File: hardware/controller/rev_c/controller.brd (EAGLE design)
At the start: 68.1 x 80 mm, 106 parts, among them J1 DM3AT-SF-PEJM5, J10 SOLDERJUMPERTRACE, J11 SOLDERJUMPERTRACE, J12 SOLDERJUMPERTRACE, J14 TC2030-JLINK-L, J15 TC2030-JLINK-L, J16 U.FL-R-SMT, J2 MICRO_USB_B_HIROSE_ZX62R-B-5P, J3 MICRO_USB_B_HIROSE_ZX62R-B-5P, J4 MODULE_CONTROLLER, J9 SOLDERJUMPERTRACE, Q1 DMN32D2LDF, SW1 B3U-1000P, SW2 B3U-1000P, SW3 SIP3240X, SW4 SIP3240X, SW5 SIP3240X, SW6 B3U-1000P, SW7 B3U-1000P, U1 FM25CLXXB-DG, U2 FTDI234XD, U3 RXM-GPS-RM-T, U33 NCP301LSN30, U4 SAM4LC8BA, U5 SAM4LC8BA, U6 SN74LVC1G125DBVR, U7 TS3USB30E, U8 TXS0108EVQFN20, U9 NCP301LSN30, X1 16MHz, X2 16MHz

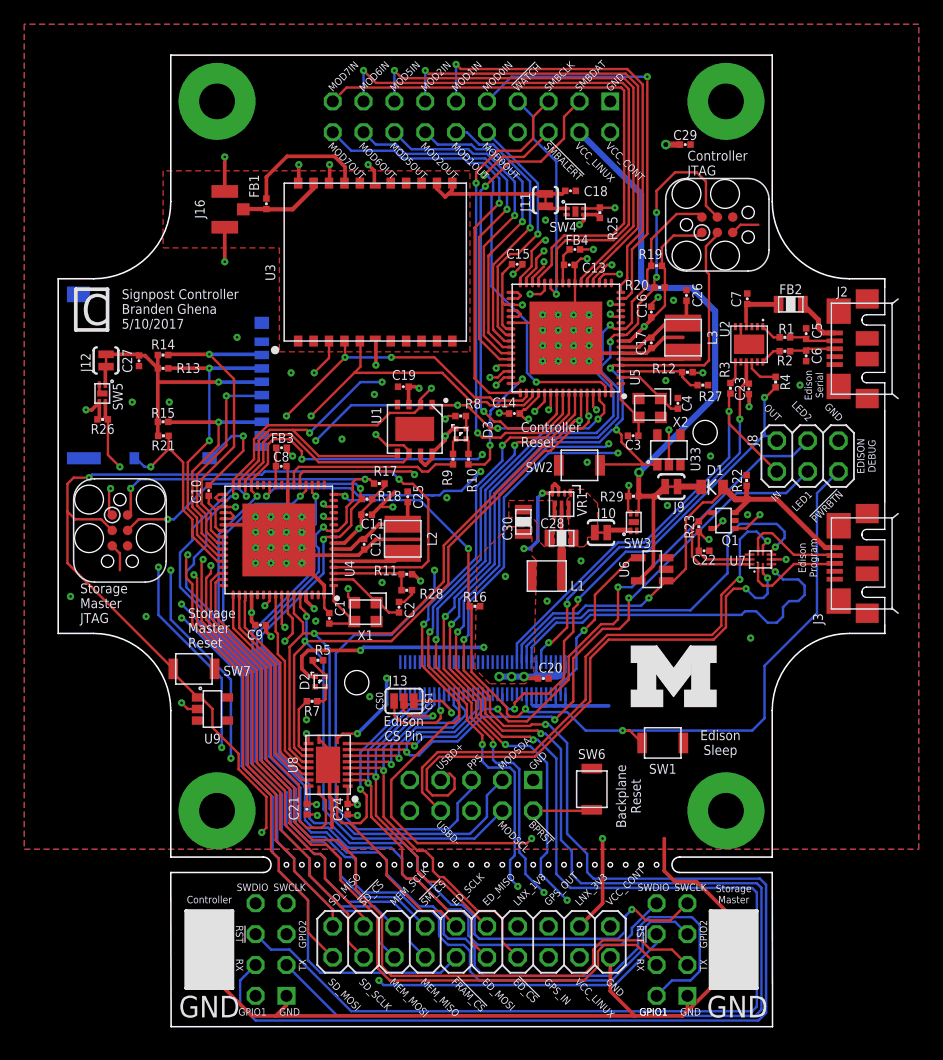
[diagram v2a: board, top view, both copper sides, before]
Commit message: Renumbered parts
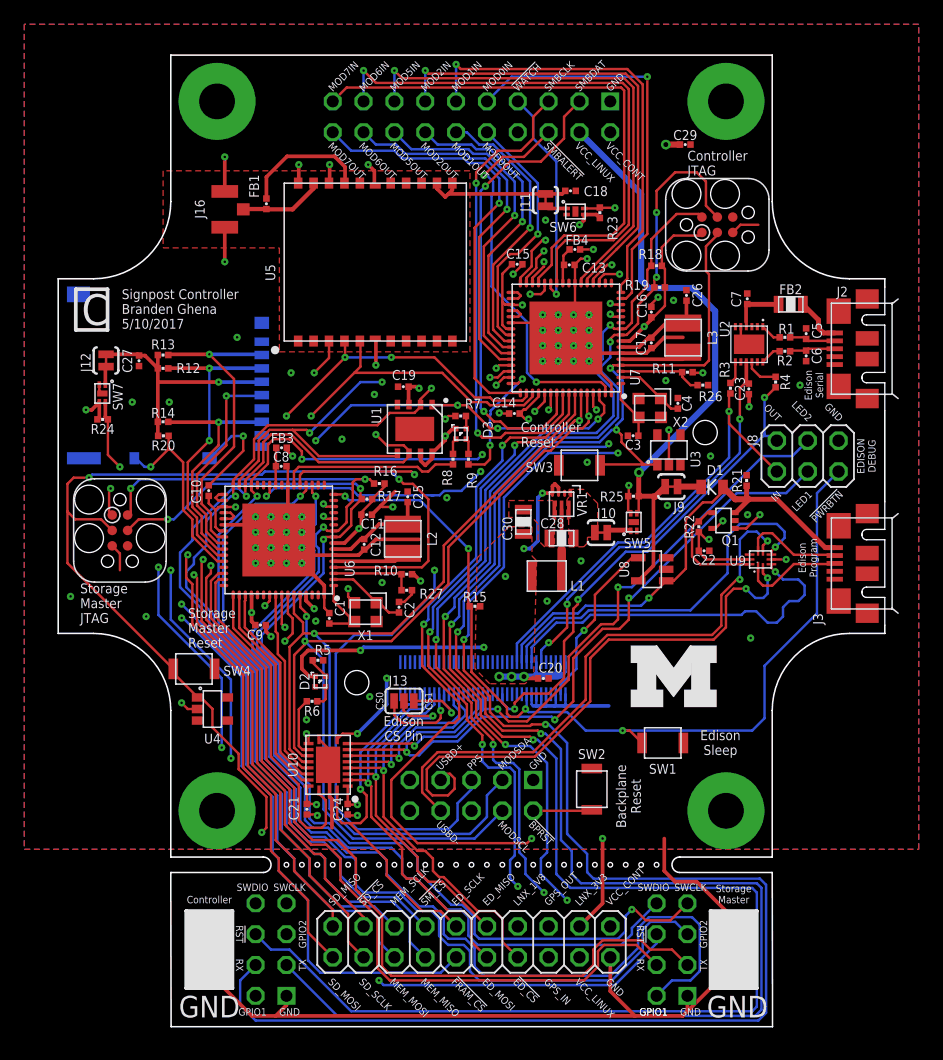
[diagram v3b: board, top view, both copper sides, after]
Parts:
- removed R28: DNP, passives:0402_RES
- removed R29: 1MΩ, passives:0402_RES
- removed U33: NCP301LSN30, signpost:SOT23-5
- added R24: 1MΩ, passives:0402_RES
- added R6: 1kΩ, passives:0402_RES
- added U10: TXS0108EVQFN20, chips:R-PVQFN-N20
- R10: value 1kΩ -> 10kΩ
- R16: value 10kΩ -> 100kΩ
- R23: value 100kΩ -> 1MΩ
- R26: value 1MΩ -> DNP
- SW3, SW4: value SIP3240X -> B3U-1000P; device signpost:TDFN4 -> switches:B3U-1000P
- SW6, SW7: value B3U-1000P -> SIP3240X; device switches:B3U-1000P -> signpost:TDFN4
- U3: value RXM-GPS-RM-T -> NCP301LSN30; device chips:RXM-GPS-RM-T -> signpost:SOT23-5
- U4: value SAM4LC8BA -> NCP301LSN30; device chips:QFN-64-9MM -> signpost:SOT23-5
- U5: value SAM4LC8BA -> RXM-GPS-RM-T; device chips:QFN-64-9MM -> chips:RXM-GPS-RM-T
- U6: value SN74LVC1G125DBVR -> SAM4LC8BA; device chips:SOT-23-5 -> chips:QFN-64-9MM
- U7: value TS3USB30E -> SAM4LC8BA; device signpost:UQFN-10 -> chips:QFN-64-9MM
- U8: value TXS0108EVQFN20 -> SN74LVC1G125DBVR; device chips:R-PVQFN-N20 -> chips:SOT-23-5
- U9: value NCP301LSN30 -> TS3USB30E; device signpost:SOT23-5 -> signpost:UQFN-10
- moved R26 49.5 mm to (19.1, 5.84)
- moved SW4 49.1 mm to (-22.9, -17.5), turned to 0 degrees
- moved R21 48.2 mm to (22.7, -2.01), turned to 90 degrees
- moved SW6 47.6 mm to (8.56, 20.1), turned to 270 degrees
- moved U9 46.8 mm to (23.8, -8.51), turned to 0 degrees
- moved SW5 45.0 mm to (13.4, -5.44), turned to 0 degrees
- moved R12 43.2 mm to (-25.4, 7.22), turned to 180 degrees
- moved R20 42.7 mm to (-25.4, 1.67), turned to 180 degrees
- moved U8 31.2 mm to (14.9, -9.32)
- moved U6 30.9 mm to (-15.9, -6.91), turned to 180 degrees
- moved R18 30.6 mm to (15.2, 15.7)
- moved R15 29.8 mm to (0.28, -12.4), turned to 0 degrees
- moved R27 29.7 mm to (-5.33, -11.0)
- moved U3 28.7 mm to (16.3, 0.51), turned to 180 degrees
- moved R11 28.5 mm to (17.8, 6.91)
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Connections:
- net !BACKPLANE_RESET: now also SW2.1, U6.58; no longer SW6.1, U4.58
- net !CONTROLLER_LED: now also R9.2, U7.48; no longer R10.2, U5.48
- net !CONTROLLER_RESET: now also SW3.1, U3.1, U7.4; no longer SW2.1, U33.1, U5.4
- net !EDISON_PWRBTN: now also R15.1, U6.16; no longer R16.1, U4.16
- net !EDISON_SPI_CS: now also U10.16, U6.56; no longer U4.56, U8.16
- net !EDISON_SPI_CS_1V8: now also U10.5; no longer U8.5
- net !ENABLE_LINUX: now also U6.21; no longer U4.21
- net !FRAM_CS: now also U7.62; no longer U5.62
- net !SD_CS: now also R13.1, U6.40; no longer R14.1, U4.40
- net !SD_DETECT: now also R20.1, U6.44; no longer R21.1, U4.44
- net !SMBALERT: now also U7.63; no longer U5.63
- net !STORAGE_CS: now also U6.29, U7.54; no longer U4.29, U5.54
- net !STORAGE_LED: now also R8.2, U6.22; no longer R9.2, U4.22
- net !STORAGE_RESET: now also SW4.1, U4.1, U6.4; no longer SW7.1, U4.4, U9.1
- net !WATCHDOG: now also U7.27; no longer U5.27
- net CONTROLLER_BUCK/LDO_N: now also R11.1, R26.2, U7.3; no longer R12.1, R27.2, U5.3
- net CONTROLLER_DEBUG_GPIO1: now also U7.57; no longer U5.57
- net CONTROLLER_DEBUG_GPIO2: now also U7.58; no longer U5.58
- net CONTROLLER_DEBUG_RX: now also U7.19; no longer U5.19
- net CONTROLLER_DEBUG_TX: now also U7.20; no longer U5.20
- net CONTROLLER_SWDCLK: now also R19.1, U7.9; no longer R20.1, U5.9
- net CONTROLLER_SWDIO: now also R18.1, U7.10; no longer R19.1, U5.10
- net CONTROLLER_XIN: now also U7.1; no longer U5.1
- net CONTROLLER_XOUT: now also U7.2; no longer U5.2
- net EDISON_INTERRUPT: now also U10.12, U6.57; no longer U4.57, U8.12
- net EDISON_INTERRUPT_1V8: now also U10.9; no longer U8.9
- net EDISON_LED1: now also U10.8; no longer U8.8
- net EDISON_SPI_MISO: now also U10.17, U6.51; no longer U4.51, U8.17
- net EDISON_SPI_MISO_1V8: now also U10.4; no longer U8.4
- net EDISON_SPI_MOSI: now also U10.18, U6.50; no longer U4.50, U8.18
- net EDISON_SPI_MOSI_1V8: now also U10.3; no longer U8.3
- net EDISON_SPI_SCLK: now also U10.20, U6.49; no longer U4.49, U8.20
- net EDISON_SPI_SCLK_1V8: now also U10.1; no longer U8.1
- net GND: now also R21.2, R26.1, R7.2, SW6.PAD, SW7.PAD, U10.11, U10.THERMAL, U3.3, U4.3, U5.18, U5.20, U5.21, U5.22, U6.23, U6.38, U6.6, U6.64, U6.GND, U7.23, U7.38, U7.6, U7.64, U7.GND, U8.2, U8.3, U9.4, U9.8; no longer R22.2, R28.1, R8.2, SW3.PAD, SW4.PAD, U3.18, U3.20, U3.21, U3.22, U33.3, U4.23, U4.38, U4.6, U4.64, U4.GND, U5.23, U5.38, U5.6, U5.64, U5.GND, U6.2, U6.3, U7.4, U7.8, U8.11, U8.THERMAL, U9.3
- net GPS_ENABLE_POWER: now also R23.1, SW6.4, U7.28; no longer R25.1, SW4.4, U5.28
- net GPS_IN_RX: now also U5.5, U7.51; no longer U3.5, U5.51
- net GPS_OUT_TX: now also U5.4, U7.50; no longer U3.4, U5.50
- net LINUX_ENABLE_POWER: now also R25.1, SW5.4; no longer R29.1, SW3.4
- net MEMORY_MISO: now also U6.32, U7.31; no longer U4.32, U5.31
- net MEMORY_MOSI: now also U6.31, U7.32; no longer U4.31, U5.32
- net MEMORY_SCLK: now also U6.30, U7.30; no longer U4.30, U5.30
- net MOD0_IN: now also U7.15; no longer U5.15
- net MOD0_OUT: now also U7.40; no longer U5.40
- net MOD1_IN: now also U7.16; no longer U5.16
- net MOD1_OUT: now also U7.41; no longer U5.41
- net MOD2_IN: now also U7.21; no longer U5.21
- net MOD2_OUT: now also U7.42; no longer U5.42
- net MOD5_IN: now also U7.22; no longer U5.22
- net MOD5_OUT: now also U7.43; no longer U5.43
- net MOD6_IN: now also U7.26; no longer U5.26
- net MOD6_OUT: now also U7.44; no longer U5.44
- net MOD7_IN: now also U7.29; no longer U5.29
- net MOD7_OUT: now also U7.49; no longer U5.49
- net MODSTORAGE_IN: now also U6.14, U7.46; no longer U4.14, U5.46
- net MODSTORAGE_OUT: now also U6.12, U7.47; no longer U4.12, U5.47
- net MODULES_SCL: now also U10.14, U6.60, U7.12, U7.60; no longer U4.60, U5.12, U5.60, U8.14
- net MODULES_SCL_1V8: now also U10.7; no longer U8.7
- net MODULES_SDA: now also U10.15, U6.59, U7.14, U7.59; no longer U4.59, U5.14, U5.59, U8.15
- net MODULES_SDA_1V8: now also U10.6; no longer U8.6
- net N$1: now also U5.17; no longer U3.17
- net N$16: now also SW5.1; no longer SW3.1
- net N$17: now also U8.4; no longer U6.4
- net N$18: now also SW7.1; no longer SW5.1
- net N$19: now also SW6.1; no longer SW4.1
- net N$29: now also U6.25; no longer U4.25
- net N$3: now also U5.19; no longer U3.19
- net N$30: now also R22.2, U9.10; no longer R23.2, U7.10
- net N$32: now also U7.25; no longer U5.25
- net N$38: now also R6.1; no longer R7.1
- net N$44: now also U7.7; no longer U5.7
- net N$45: now also U6.7; no longer U4.7
- net N$46: now also U6.5; no longer U4.5
- net N$48: now also U6.33, U6.34; no longer U4.33, U4.34
- net N$5: now also U9.7; no longer U7.7
- net N$50: now also R6.2, U10.13; no longer R7.2, U8.13
- net N$51: now also U6.36, U6.37; no longer U4.36, U4.37
- net N$53: now also U7.36, U7.37; no longer U5.36, U5.37
- net N$54: now also U7.33, U7.34; no longer U5.33, U5.34
- net N$56: now also U5.11, U5.12; no longer U3.11, U3.12
- net N$58: now also R12.2, R20.2; no longer R15.2, R21.2
- net N$59: now also U7.5; no longer U5.5
- net N$6: now also U9.1; no longer U7.1
- net N$7: now also R7.1; no longer R8.1
- net N$8: now also R8.1; no longer R9.1
- net N$9: now also R9.1; no longer R10.1
- net PPS: now also U5.3, U7.45; no longer U3.3, U5.45
- net SD_ENABLE_POWER: now also R24.1, SW7.4, U6.55; no longer R26.1, SW5.4, U4.55
- net SD_MISO: now also R14.1, U6.42; no longer R15.1, U4.42
- net SD_MOSI: now also R12.1, U6.43; no longer R13.1, U4.43
- net SD_SCLK: now also U6.41; no longer U4.41
- net SMBCLK: now also U7.56; no longer U5.56
- net SMBDATA: now also U7.55; no longer U5.55
- net STORAGE_BUCK/LDO_N: now also R10.1, R27.2, U6.3; no longer R11.1, R28.2, U4.3
- net STORAGE_DEBUG_GPIO1: now also U6.19; no longer U4.19
- net STORAGE_DEBUG_GPIO2: now also U6.20; no longer U4.20
- net STORAGE_DEBUG_RX: now also U6.46; no longer U4.46
- net STORAGE_DEBUG_TX: now also U6.47; no longer U4.47
- net STORAGE_INTERRUPT: now also U6.26, U7.53; no longer U4.26, U5.53
- net STORAGE_SWDCLK: now also R17.1, U6.9; no longer R18.1, U4.9
- net STORAGE_SWDIO: now also R16.1, U6.10; no longer R17.1, U4.10
- net STORAGE_XIN: now also U6.1; no longer U4.1
- net STORAGE_XOUT: now also U6.2; no longer U4.2
- net USB_D+: now also U9.3; no longer U7.3
- net USB_D-: now also U9.5; no longer U7.5
- net USB_MOD_D+: now also U9.2; no longer U7.2
- net USB_MOD_D-: now also U9.6; no longer U7.6
- net USB_VBUS: now also R21.1, U8.1; no longer R22.1, U6.1
- net VCC_CONTROLLER: now also R10.2, R16.2, R23.2, R24.2, SW6.3, SW7.3, U3.2, U4.2, U6.35, U6.39, U6.52, U6.61, U6.8, U7.35, U7.39, U7.52, U7.61, U7.8; no longer R12.2, R20.2, R25.2, R26.2, SW4.3, SW5.3, U33.2, U4.35, U4.39, U4.52, U4.61, U4.8, U5.35, U5.39, U5.52, U5.61, U5.8, U9.2
- net VCC_LINUX: now also R25.2, SW5.3, U8.5; no longer R29.2, SW3.3, U6.5
- net VCC_LINUX_1V8: now also U10.10, U10.2; no longer U8.10, U8.2
- net VCC_LINUX_3V3: now also R15.2, R22.1, U10.19, U9.9; no longer R16.2, R23.1, U7.9, U8.19

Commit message: Added updates from Pat & Josh
Pulldown on 1v8 output enable
PPS connection to storage master

Did NOT add module in/out pins for the edison
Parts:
- added R28: 100kΩ, passives:0402_RES
- moved C23 1.02 mm to (23.9, 5.54)
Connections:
- net GND: now also R28.2
- net PPS: now also U6.45
- net VCC_LINUX_1V8: now also R28.1
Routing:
- net PPS: track 76.8 -> 98.8 mm, vias 3 -> 4
- net VCC_LINUX_1V8: track 84.0 -> 85.1 mm
- net GND: track 201.9 -> 200.9 mm, vias 79 -> 78
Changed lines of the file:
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@@
 <attribute name="NAME" x="19.1516" y="-8.9408" size="0.8128" layer="25" font="vector" ratio="12" align="bottom-center"/>
 </element>
-<element name="C23" library="passives" package="0402_CAP" value="100nF" x="22.836" y="5.5372" smashed="yes" rot="R270">
-<attribute name="DIGIKEY" value="490-10777-1-ND" x="22.836" y="4.2672" size="1.778" layer="27" rot="R270" display="off"/>
-<attribute name="NAME" x="21.693" y="5.5372" size="0.8128" layer="25" font="vector" ratio="12" rot="R270" align="bottom-center"/>
+<element name="C23" library="passives" package="0402_CAP" value="100nF" x="23.852" y="5.5372" smashed="yes" rot="R270">
+<attribute name="DIGIKEY" value="490-10777-1-ND" x="23.852" y="4.2672" size="1.778" layer="27" rot="R270" display="off"/>
+<attribute name="NAME" x="22.963" y="3.7592" size="0.8128" layer="25" font="vector" ratio="12" rot="R270" align="bottom-center"/>
 </element>
 <element name="C7" library="passives" package="0402_CAP" value="10nF" x="22.709" y="12.954" smashed="yes" rot="R90">
@@
 <attribute name="NAME" x="-21.336" y="-22.86" size="0.8128" layer="25" font="vector" ratio="12" rot="R180" align="bottom-center"/>
 <attribute name="VALUE" x="-21.336" y="-18.796" size="1.016" layer="27" font="vector" ratio="12" align="bottom-center"/>
+</element>
+<element name="R28" library="passives" package="0402_RES" value="100kΩ" x="22.86" y="5.461" smashed="yes" rot="R270">
+<attribute name="DIGIKEY" value="1276-3432-1-ND" x="22.86" y="4.953" size="1.778" layer="27" rot="R270" display="off"/>
+<attribute name="NAME" x="21.717" y="4.699" size="0.8128" layer="25" font="vector" ratio="12" rot="R270" align="bottom-center"/>
+<attribute name="VALUE" x="21.463" y="5.461" size="1.016" layer="27" font="vector" ratio="12" rot="R270" align="bottom-center"/>
 </element>
 </elements>
@@
 <wire x1="22.86" y1="9.2075" x2="22.18" y2="9.8875" width="0.2032" layer="1"/>
 <wire x1="22.18" y1="9.8875" x2="22.18" y2="10.6575" width="0.2032" layer="1"/>
-<wire x1="22.836" y1="5.10413125" x2="22.86" y2="5.08013125" width="0.3048" layer="1"/>
-<wire x1="22.86" y1="5.08013125" x2="22.86" y2="4.064" width="0.3048" layer="1"/>
-<via x="22.86" y="4.064" extent="1-16" drill="0.2032"/>
 <wire x1="-20.32" y1="21.795" x2="-20.32" y2="24.638" width="0.3048" layer="1"/>
 <via x="-20.32" y="24.638" extent="1-16" drill="0.2032"/>
@@
 <wire x1="3.09753125" y1="3.5052" x2="2.3368" y2="3.5052" width="0.2032" layer="1"/>
 <wire x1="2.3368" y1="3.5052" x2="2.286" y2="3.556" width="0.2032" layer="1"/>
+<contactref element="R28" pad="2"/>
 </signal>
 <signal name="PPS">
@@
 <wire x1="-11.7348" y1="8.0772" x2="-12.954" y2="6.858" width="0.2032" layer="1"/>
 <via x="-12.954" y="6.858" extent="1-16" drill="0.2032"/>
-<wire x1="-12.954" y1="6.858" x2="0.254" y2="6.858" width="0.2032" layer="2"/>
+<wire x1="0.254" y1="6.858" x2="-12.954" y2="6.858" width="0.2032" layer="2"/>
 <via x="2.032" y="7.239" extent="1-16" drill="0.2032"/>
 <wire x1="-3.048" y1="-9.398" x2="-3.048" y2="-6.604" width="0.2032" layer="2"/>
@@
 <wire x1="2.032" y1="7.239" x2="0.635" y2="7.239" width="0.2032" layer="2"/>
 <wire x1="0.635" y1="7.239" x2="0.254" y2="6.858" width="0.2032" layer="2"/>
+<contactref element="U6" pad="45"/>
+<wire x1="-12.954" y1="6.858" x2="-12.954" y2="3.83826875" width="0.2032" layer="2"/>
+<wire x1="-12.2682" y1="-1.7018" x2="-12.192" y2="-1.778" width="0.2032" layer="2"/>
+<wire x1="-12.954" y1="3.83826875" x2="-12.2682" y2="3.15246875" width="0.2032" layer="2"/>
+<wire x1="-12.2682" y1="3.15246875" x2="-12.2682" y2="-1.7018" width="0.2032" layer="2"/>
+<wire x1="-12.192" y1="-1.778" x2="-13.1572" y2="-2.7432" width="0.2032" layer="2"/>
+<wire x1="-13.1572" y1="-2.7432" x2="-14.32846875" y2="-2.7432" width="0.2032" layer="2"/>
+<wire x1="-15.44606875" y1="-3.8608" x2="-17.78" y2="-3.8608" width="0.2032" layer="2"/>
+<wire x1="-17.78" y1="-3.8608" x2="-19.431" y2="-5.5118" width="0.2032" layer="2"/>
+<wire x1="-14.32846875" y1="-2.7432" x2="-15.44606875" y2="-3.8608" width="0.2032" layer="2"/>
+<via x="-19.431" y="-8.636" extent="1-16" drill="0.2032"/>
+<wire x1="-19.431" y1="-5.5118" x2="-19.431" y2="-8.636" width="0.2032" layer="2"/>
+<wire x1="-20.4" y1="-9.1588" x2="-19.9538" y2="-9.1588" width="0.2032" layer="1"/>
+<wire x1="-19.9538" y1="-9.1588" x2="-19.431" y2="-8.636" width="0.2032" layer="1"/>
 </signal>
 <signal name="N$1">
@@
 <via x="3.556" y="-20.828" extent="1-16" drill="0.2032"/>
 <via x="8.763" y="-11.811" extent="1-16" drill="0.2032"/>
-<via x="24.13" y="4.826" extent="1-16" drill="0.2032"/>
 <wire x1="8.763" y1="-11.811" x2="12.7" y2="-7.874" width="0.2032" layer="16"/>
 <wire x1="12.7" y1="-7.874" x2="14.478" y2="-7.874" width="0.2032" layer="16"/>
 <contactref element="J8" pad="5"/>
 <wire x1="14.478" y1="-7.874" x2="24.003" y2="1.651" width="0.2032" layer="16"/>
-<wire x1="24.003" y1="1.651" x2="24.13" y2="1.778" width="0.2032" layer="16"/>
-<wire x1="24.13" y1="1.778" x2="24.13" y2="4.826" width="0.2032" layer="16"/>
 <wire x1="25.146" y1="1.27" x2="24.765" y2="1.651" width="0.2032" layer="16"/>
 <wire x1="24.765" y1="1.651" x2="24.003" y2="1.651" width="0.2032" layer="16"/>
@@
 <wire x1="8.382" y1="-12.573" x2="8.763" y2="-12.192" width="0.2032" layer="1"/>
 <wire x1="8.763" y1="-12.192" x2="8.763" y2="-11.811" width="0.2032" layer="1"/>
-<wire x1="25.0444" y1="5.66293125" x2="24.20746875" y2="4.826" width="0.2032" layer="1"/>
-<wire x1="24.20746875" y1="4.826" x2="24.13" y2="4.826" width="0.2032" layer="1"/>
+<wire x1="25.4" y1="3.048" x2="25.4" y2="4.318" width="0.2032" layer="16"/>
+<via x="25.4" y="4.318" extent="1-16" drill="0.2032"/>
+<wire x1="25.4" y1="4.318" x2="25.0444" y2="4.6736" width="0.2032" layer="1"/>
+<wire x1="25.0444" y1="4.6736" x2="25.0444" y2="5.66293125" width="0.2032" layer="1"/>
+<wire x1="24.003" y1="1.651" x2="25.4" y2="3.048" width="0.2032" layer="16"/>
 </signal>
 <signal name="N$28">
@@
 <contactref element="C24" pad="2"/>
 <contactref element="J7" pad="14"/>
-<wire x1="22.63" y1="7.7575" x2="22.63" y2="6.17626875" width="0.3048" layer="1"/>
-<wire x1="22.63" y1="6.17626875" x2="22.836" y2="5.97026875" width="0.3048" layer="1"/>
 <wire x1="-10.1985" y1="-27.1754" x2="-10.1985" y2="-28.64993125" width="0.2032" layer="1"/>
 <wire x1="-10.1985" y1="-28.64993125" x2="-10.14643125" y2="-28.702" width="0.2032" layer="1"/>
@@
 <via x="22.098" y="3.048" extent="1-16" drill="0.2032"/>
 <wire x1="22.098" y1="3.048" x2="22.098" y2="5.588" width="0.2032" layer="1"/>
-<wire x1="22.098" y1="5.588" x2="22.48026875" y2="5.97026875" width="0.2032" layer="1"/>
-<wire x1="22.48026875" y1="5.97026875" x2="22.836" y2="5.97026875" width="0.2032" layer="1"/>
 <wire x1="6.35" y1="-17.931609375" x2="6.35" y2="-15.367" width="0.3048" layer="15"/>
 <wire x1="6.35" y1="-17.931609375" x2="4.977609375" y2="-19.304" width="0.3048" layer="15"/>
@@
 <wire x1="7.874" y1="-14.097" x2="6.604" y2="-15.367" width="0.2032" layer="1"/>
 <wire x1="6.604" y1="-15.367" x2="6.35" y2="-15.367" width="0.2032" layer="1"/>
+<contactref element="R28" pad="1"/>
+<wire x1="22.40406875" y1="5.89406875" x2="22.098" y2="5.588" width="0.2032" layer="1"/>
+<wire x1="22.40406875" y1="5.89406875" x2="22.86" y2="5.89406875" width="0.2032" layer="1"/>
+<wire x1="22.63" y1="7.7575" x2="22.63" y2="6.12406875" width="0.2032" layer="1"/>
+<wire x1="22.63" y1="6.12406875" x2="22.86" y2="5.89406875" width="0.2032" layer="1"/>
+<wire x1="22.86" y1="5.89406875" x2="23.7758" y2="5.89406875" width="0.2032" layer="1"/>
+<wire x1="23.7758" y1="5.89406875" x2="23.852" y2="5.97026875" width="0.2032" layer="1"/>
 </signal>
 <signal name="N$34">
